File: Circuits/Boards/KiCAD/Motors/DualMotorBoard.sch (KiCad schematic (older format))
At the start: 0 parts

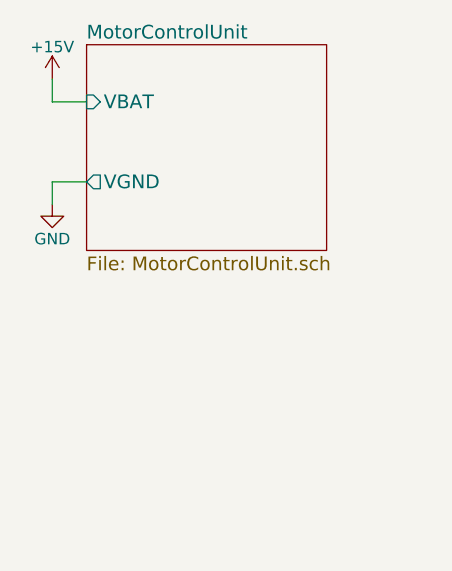
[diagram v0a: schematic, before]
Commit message: Created subcircuit for motor control and routing dual controller
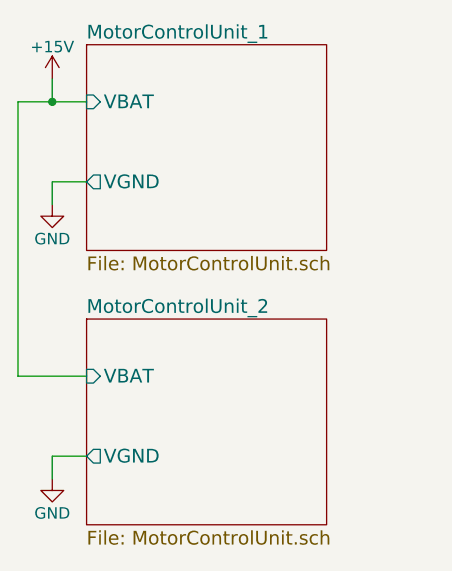
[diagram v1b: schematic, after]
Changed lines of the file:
@@
 LIBS:contrib
 LIBS:valves
-LIBS:SingleMotorBoard-cache
+LIBS:DualMotorBoard-cache
 EELAYER 25 0
 EELAYER END
 $Descr A4 11693 8268
 encoding utf-8
-Sheet 1 2
+Sheet 1 3
 Title ""
 Date ""
@@
 S 5400 1850 1050 900
 U 5A51075D
-F0 "MotorControlUnit" 60
+F0 "MotorControlUnit_1" 60
 F1 "MotorControlUnit.sch" 60
 F2 "VBAT" I L 5400 2100 60
@@
 	5250 2000 5250 2100
 Wire Wire Line
-	5250 2100 5400 2100
+	5100 2100 5400 2100
+$Sheet
+S 5400 3050 1050 900
+U 5A5113FC
+F0 "MotorControlUnit_2" 60
+F1 "MotorControlUnit.sch" 60
+F2 "VBAT" I L 5400 3300 60
+F3 "VGND" O L 5400 3650 60
+$EndSheet
+$Comp
+L GND #PWR03
+U 1 1 5A511402
+P 5250 3750
+F 0 "#PWR03" H 5250 3500 50  0001 C CNN
+F 1 "GND" H 5250 3600 50  0000 C CNN
+F 2 "" H 5250 3750 50  0001 C CNN
+F 3 "" H 5250 3750 50  0001 C CNN
+	1    5250 3750
+	1    0    0    -1
+$EndComp
+Wire Wire Line
+	5400 3650 5250 3650
+Wire Wire Line
+	5250 3650 5250 3750
+Wire Wire Line
+	5100 3300 5400 3300
+Wire Wire Line
+	5100 2100 5100 3300
+Connection ~ 5250 2100
 $EndSCHEMATC

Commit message: Added 26V and 5V units to the Dual motor controller board
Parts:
- added F1, F12, F13: Polyfuse, Resistors_THT:R_Axial_DIN0207_L6.3mm_D2.5mm_P7.62mm_Horizontal, symbol Polyfuse
- added J15, J16: Conn_01x02, Connectors_JST:JST_XH_B02B-XH-A_02x2.50mm_Straight, symbol Conn_01x02
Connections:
- wire segments 8 -> 30

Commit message: Fixed missing connections and routing
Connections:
- net labels added: +BATT
- net labels removed: +15V
- wire segments 30 -> 32
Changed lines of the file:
@@
 $EndSheet
 $Comp
-L GND #PWR2
+L GND #PWR01
 U 1 1 5A5181EA
 P 4150 2500
-F 0 "#PWR2" H 4150 2250 50  0001 C CNN
+F 0 "#PWR01" H 4150 2250 50  0001 C CNN
 F 1 "GND" H 4150 2350 50  0000 C CNN
 F 2 "" H 4150 2500 50  0001 C CNN
 F 3 "" H 4150 2500 50  0001 C CNN
 	1    4150 2500
-	1    0    0    -1
-$EndComp
-$Comp
-L +15V #PWR1
-U 1 1 5A5182E1
-P 4150 1950
-F 0 "#PWR1" H 4150 1800 50  0001 C CNN
-F 1 "+15V" H 4150 2090 50  0000 C CNN
-F 2 "" H 4150 1950 50  0001 C CNN
-F 3 "" H 4150 1950 50  0001 C CNN
-	1    4150 1950
 	1    0    0    -1
 $EndComp
@@
 $EndSheet
 $Comp
-L GND #PWR4
+L GND #PWR02
 U 1 1 5A511402
 P 4150 3700
-F 0 "#PWR4" H 4150 3450 50  0001 C CNN
+F 0 "#PWR02" H 4150 3450 50  0001 C CNN
 F 1 "GND" H 4150 3550 50  0000 C CNN
 F 2 "" H 4150 3700 50  0001 C CNN
@@
 $EndSheet
 $Comp
-L +15V #PWR3
-U 1 1 5A51EDDB
-P 4150 3150
-F 0 "#PWR3" H 4150 3000 50  0001 C CNN
-F 1 "+15V" H 4150 3290 50  0000 C CNN
-F 2 "" H 4150 3150 50  0001 C CNN
-F 3 "" H 4150 3150 50  0001 C CNN
-	1    4150 3150
-	1    0    0    -1
-$EndComp
-$Comp
-L GND #PWR5
+L GND #PWR03
 U 1 1 5A51F50D
 P 7050 2550
-F 0 "#PWR5" H 7050 2300 50  0001 C CNN
+F 0 "#PWR03" H 7050 2300 50  0001 C CNN
 F 1 "GND" H 7050 2400 50  0000 C CNN
 F 2 "" H 7050 2550 50  0001 C CNN
@@
 $EndComp
 $Comp
-L GND #PWR6
+L GND #PWR04
 U 1 1 5A521A49
 P 7050 3700
-F 0 "#PWR6" H 7050 3450 50  0001 C CNN
+F 0 "#PWR04" H 7050 3450 50  0001 C CNN
 F 1 "GND" H 7050 3550 50  0000 C CNN
 F 2 "" H 7050 3700 50  0001 C CNN
@@
 $EndComp
 $Comp
-L GND #PWR7
+L GND #PWR05
 U 1 1 5A5276C7
 P 8900 2800
-F 0 "#PWR7" H 8900 2550 50  0001 C CNN
+F 0 "#PWR05" H 8900 2550 50  0001 C CNN
 F 1 "GND" H 8900 2650 50  0000 C CNN
 F 2 "" H 8900 2800 50  0001 C CNN
@@
 Wire Wire Line
 	6000 2950 6100 2950
+$Comp
+L GND #PWR06
+U 1 1 5A520157
+P 3050 2550
+F 0 "#PWR06" H 3050 2300 50  0001 C CNN
+F 1 "GND" H 3050 2400 50  0000 C CNN
+F 2 "" H 3050 2550 50  0001 C CNN
+F 3 "" H 3050 2550 50  0001 C CNN
+	1    3050 2550
+	1    0    0    -1
+$EndComp
+$Comp
+L +BATT #PWR07
+U 1 1 5A5202E3
+P 4150 1950
+F 0 "#PWR07" H 4150 1800 50  0001 C CNN
+F 1 "+BATT" H 4150 2090 50  0000 C CNN
+F 2 "" H 4150 1950 50  0001 C CNN
+F 3 "" H 4150 1950 50  0001 C CNN
+	1    4150 1950
+	1    0    0    -1
+$EndComp
+$Comp
+L +BATT #PWR08
+U 1 1 5A520413
+P 4150 3150
+F 0 "#PWR08" H 4150 3000 50  0001 C CNN
+F 1 "+BATT" H 4150 3290 50  0000 C CNN
+F 2 "" H 4150 3150 50  0001 C CNN
+F 3 "" H 4150 3150 50  0001 C CNN
+	1    4150 3150
+	1    0    0    -1
+$EndComp
+$Comp
+L PWR_FLAG #FLG09
+U 1 1 5A520961
+P 3050 2400
+F 0 "#FLG09" H 3050 2475 50  0001 C CNN
+F 1 "PWR_FLAG" H 3050 2550 50  0000 C CNN
+F 2 "" H 3050 2400 50  0001 C CNN
+F 3 "" H 3050 2400 50  0001 C CNN
+	1    3050 2400
+	1    0    0    -1
+$EndComp
+Wire Wire Line
+	3050 2400 3050 2550
+$Comp
+L +BATT #PWR010
+U 1 1 5A520B60
+P 2700 2400
+F 0 "#PWR010" H 2700 2250 50  0001 C CNN
+F 1 "+BATT" H 2700 2540 50  0000 C CNN
+F 2 "" H 2700 2400 50  0001 C CNN
+F 3 "" H 2700 2400 50  0001 C CNN
+	1    2700 2400
+	1    0    0    -1
+$EndComp
+$Comp
+L PWR_FLAG #FLG011
+U 1 1 5A520BDA
+P 2700 2550
+F 0 "#FLG011" H 2700 2625 50  0001 C CNN
+F 1 "PWR_FLAG" H 2700 2700 50  0000 C CNN
+F 2 "" H 2700 2550 50  0001 C CNN
+F 3 "" H 2700 2550 50  0001 C CNN
+	1    2700 2550
+	-1   0    0    1
+$EndComp
+Wire Wire Line
+	2700 2400 2700 2550
+$Comp
+L PWR_FLAG #FLG?
+U 1 1 5A523699
+P 8450 2100
+F 0 "#FLG?" H 8450 2175 50  0001 C CNN
+F 1 "PWR_FLAG" H 8450 2250 50  0000 C CNN
+F 2 "" H 8450 2100 50  0001 C CNN
+F 3 "" H 8450 2100 50  0001 C CNN
+	1    8450 2100
+	1    0    0    -1
+$EndComp
 $EndSCHEMATC

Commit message: Added pin outputs for battery to ground (for external connections)
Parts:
- added F14, F15, F16, F17: Polyfuse, Resistors_THT:R_Axial_DIN0207_L6.3mm_D2.5mm_P7.62mm_Horizontal, symbol Polyfuse
- added J18, J19: Conn_01x02, Connectors_JST:JST_XH_B02B-XH-A_02x2.50mm_Straight, symbol Conn_01x02
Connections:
- wire segments 32 -> 40
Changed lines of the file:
@@
 LIBS:contrib
 LIBS:valves
+LIBS:DualMotorBoard-cache
 EELAYER 25 0
 EELAYER END
@@
 $EndSheet
 $Comp
-L GND #PWR01
+L GND #PWR8
 U 1 1 5A5181EA
 P 4150 2500
-F 0 "#PWR01" H 4150 2250 50  0001 C CNN
+F 0 "#PWR8" H 4150 2250 50  0001 C CNN
 F 1 "GND" H 4150 2350 50  0000 C CNN
 F 2 "" H 4150 2500 50  0001 C CNN
@@
 $EndSheet
 $Comp
-L GND #PWR02
+L GND #PWR10
 U 1 1 5A511402
 P 4150 3700
-F 0 "#PWR02" H 4150 3450 50  0001 C CNN
+F 0 "#PWR10" H 4150 3450 50  0001 C CNN
 F 1 "GND" H 4150 3550 50  0000 C CNN
 F 2 "" H 4150 3700 50  0001 C CNN
@@
 $EndSheet
 $Comp
-L GND #PWR03
+L GND #PWR11
 U 1 1 5A51F50D
 P 7050 2550
-F 0 "#PWR03" H 7050 2300 50  0001 C CNN
+F 0 "#PWR11" H 7050 2300 50  0001 C CNN
 F 1 "GND" H 7050 2400 50  0000 C CNN
 F 2 "" H 7050 2550 50  0001 C CNN
@@
 $EndComp
 $Comp
-L GND #PWR04
+L GND #PWR12
 U 1 1 5A521A49
 P 7050 3700
-F 0 "#PWR04" H 7050 3450 50  0001 C CNN
+F 0 "#PWR12" H 7050 3450 50  0001 C CNN
 F 1 "GND" H 7050 3550 50  0000 C CNN
 F 2 "" H 7050 3700 50  0001 C CNN
@@
 $EndComp
 $Comp
-L GND #PWR05
+L GND #PWR13
 U 1 1 5A5276C7
 P 8900 2800
-F 0 "#PWR05" H 8900 2550 50  0001 C CNN
+F 0 "#PWR13" H 8900 2550 50  0001 C CNN
 F 1 "GND" H 8900 2650 50  0000 C CNN
 F 2 "" H 8900 2800 50  0001 C CNN
@@
 	6000 2950 6100 2950
 $Comp
-L GND #PWR06
+L GND #PWR6
 U 1 1 5A520157
 P 3050 2550
-F 0 "#PWR06" H 3050 2300 50  0001 C CNN
+F 0 "#PWR6" H 3050 2300 50  0001 C CNN
 F 1 "GND" H 3050 2400 50  0000 C CNN
 F 2 "" H 3050 2550 50  0001 C CNN
@@
 $EndComp
 $Comp
-L +BATT #PWR07
+L +BATT #PWR7
 U 1 1 5A5202E3
 P 4150 1950
-F 0 "#PWR07" H 4150 1800 50  0001 C CNN
+F 0 "#PWR7" H 4150 1800 50  0001 C CNN
 F 1 "+BATT" H 4150 2090 50  0000 C CNN
 F 2 "" H 4150 1950 50  0001 C CNN
@@
 $EndComp
 $Comp
-L +BATT #PWR08
+L +BATT #PWR9
 U 1 1 5A520413
 P 4150 3150
-F 0 "#PWR08" H 4150 3000 50  0001 C CNN
+F 0 "#PWR9" H 4150 3000 50  0001 C CNN
 F 1 "+BATT" H 4150 3290 50  0000 C CNN
 F 2 "" H 4150 3150 50  0001 C CNN
@@
 $EndComp
 $Comp
-L PWR_FLAG #FLG09
+L PWR_FLAG #FLG2
 U 1 1 5A520961
 P 3050 2400
-F 0 "#FLG09" H 3050 2475 50  0001 C CNN
+F 0 "#FLG2" H 3050 2475 50  0001 C CNN
 F 1 "PWR_FLAG" H 3050 2550 50  0000 C CNN
 F 2 "" H 3050 2400 50  0001 C CNN
@@
 	3050 2400 3050 2550
 $Comp
-L +BATT #PWR010
+L +BATT #PWR5
 U 1 1 5A520B60
 P 2700 2400
-F 0 "#PWR010" H 2700 2250 50  0001 C CNN
+F 0 "#PWR5" H 2700 2250 50  0001 C CNN
 F 1 "+BATT" H 2700 2540 50  0000 C CNN
 F 2 "" H 2700 2400 50  0001 C CNN
@@
 $EndComp
 $Comp
-L PWR_FLAG #FLG011
+L PWR_FLAG #FLG1
 U 1 1 5A520BDA
 P 2700 2550
-F 0 "#FLG011" H 2700 2625 50  0001 C CNN
+F 0 "#FLG1" H 2700 2625 50  0001 C CNN
 F 1 "PWR_FLAG" H 2700 2700 50  0000 C CNN
 F 2 "" H 2700 2550 50  0001 C CNN
@@
 	2700 2400 2700 2550
 $Comp
-L PWR_FLAG #FLG012
+L PWR_FLAG #FLG3
 U 1 1 5A523699
 P 8450 2100
-F 0 "#FLG012" H 8450 2175 50  0001 C CNN
+F 0 "#FLG3" H 8450 2175 50  0001 C CNN
 F 1 "PWR_FLAG" H 8450 2250 50  0000 C CNN
 F 2 "" H 8450 2100 50  0001 C CNN
@@
 	1    0    0    -1
 $EndComp
+$Comp
+L Conn_01x02 J18
+U 1 1 5A610638
+P 3150 3200
+F 0 "J18" H 3150 3300 50  0000 C CNN
+F 1 "Conn_01x02" H 3150 3000 50  0000 C CNN
+F 2 "Connectors_JST:JST_XH_B02B-XH-A_02x2.50mm_Straight" H 3150 3200 50  0001 C CNN
+F 3 "" H 3150 3200 50  0001 C CNN
+	1    3150 3200
+	1    0    0    -1
+$EndComp
+$Comp
+L Polyfuse F14
+U 1 1 5A61063E
+P 2700 3200
+F 0 "F14" V 2600 3200 50  0000 C CNN
+F 1 "Polyfuse" V 2800 3200 50  0000 C CNN
+F 2 "Resistors_THT:R_Axial_DIN0207_L6.3mm_D2.5mm_P7.62mm_Horizontal" H 2750 3000 50  0001 L CNN
+F 3 "" H 2700 3200 50  0001 C CNN
+	1    2700 3200
+	0    1    1    0
+$EndComp
+$Comp
+L Polyfuse F15
+U 1 1 5A610644
+P 2700 3300
+F 0 "F15" V 2600 3300 50  0000 C CNN
+F 1 "Polyfuse" V 2800 3300 50  0000 C CNN
+F 2 "Resistors_THT:R_Axial_DIN0207_L6.3mm_D2.5mm_P7.62mm_Horizontal" H 2750 3100 50  0001 L CNN
+F 3 "" H 2700 3300 50  0001 C CNN
+	1    2700 3300
+	0    1    1    0
+$EndComp
+Wire Wire Line
+	2850 3300 2950 3300
+Wire Wire Line
+	2950 3200 2850 3200
+Wire Wire Line
+	2550 3200 2450 3200
+Wire Wire Line
+	2450 3300 2550 3300
+$Comp
+L +BATT #PWR1
+U 1 1 5A612841
+P 2450 3200
+F 0 "#PWR1" H 2450 3050 50  0001 C CNN
+F 1 "+BATT" H 2450 3340 50  0000 C CNN
+F 2 "" H 2450 3200 50  0001 C CNN
+F 3 "" H 2450 3200 50  0001 C CNN
+	1    2450 3200
+	1    0    0    -1
+$EndComp
+$Comp
+L GND #PWR2
+U 1 1 5A6128C4
+P 2450 3300
+F 0 "#PWR2" H 2450 3050 50  0001 C CNN
+F 1 "GND" H 2450 3150 50  0000 C CNN
+F 2 "" H 2450 3300 50  0001 C CNN
+F 3 "" H 2450 3300 50  0001 C CNN
+	1    2450 3300
+	1    0    0    -1
+$EndComp
+$Comp
+L Conn_01x02 J19
+U 1 1 5A60FE63
+P 3150 3750
+F 0 "J19" H 3150 3850 50  0000 C CNN
+F 1 "Conn_01x02" H 3150 3550 50  0000 C CNN
+F 2 "Connectors_JST:JST_XH_B02B-XH-A_02x2.50mm_Straight" H 3150 3750 50  0001 C CNN
+F 3 "" H 3150 3750 50  0001 C CNN
+	1    3150 3750
+	1    0    0    -1
+$EndComp
+$Comp
+L Polyfuse F16
+U 1 1 5A60FE69
+P 2700 3750
+F 0 "F16" V 2600 3750 50  0000 C CNN
+F 1 "Polyfuse" V 2800 3750 50  0000 C CNN
+F 2 "Resistors_THT:R_Axial_DIN0207_L6.3mm_D2.5mm_P7.62mm_Horizontal" H 2750 3550 50  0001 L CNN
+F 3 "" H 2700 3750 50  0001 C CNN
+	1    2700 3750
+	0    1    1    0
+$EndComp
+$Comp
+L Polyfuse F17
+U 1 1 5A60FE6F
+P 2700 3850
+F 0 "F17" V 2600 3850 50  0000 C CNN
+F 1 "Polyfuse" V 2800 3850 50  0000 C CNN
+F 2 "Resistors_THT:R_Axial_DIN0207_L6.3mm_D2.5mm_P7.62mm_Horizontal" H 2750 3650 50  0001 L CNN
+F 3 "" H 2700 3850 50  0001 C CNN
+	1    2700 3850
+	0    1    1    0
+$EndComp
+Wire Wire Line
+	2850 3850 2950 3850
+Wire Wire Line
+	2950 3750 2850 3750
+Wire Wire Line
+	2550 3750 2450 3750
+Wire Wire Line
+	2450 3850 2550 3850
+$Comp
+L +BATT #PWR3
+U 1 1 5A60FE79
+P 2450 3750
+F 0 "#PWR3" H 2450 3600 50  0001 C CNN
+F 1 "+BATT" H 2450 3890 50  0000 C CNN
+F 2 "" H 2450 3750 50  0001 C CNN
+F 3 "" H 2450 3750 50  0001 C CNN
+	1    2450 3750
+	1    0    0    -1
+$EndComp
+$Comp
+L GND #PWR4
+U 1 1 5A60FE7F
+P 2450 3850
+F 0 "#PWR4" H 2450 3600 50  0001 C CNN
+F 1 "GND" H 2450 3700 50  0000 C CNN
+F 2 "" H 2450 3850 50  0001 C CNN
+F 3 "" H 2450 3850 50  0001 C CNN
+	1    2450 3850
+	1    0    0    -1
+$EndComp
